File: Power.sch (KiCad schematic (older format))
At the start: 0 parts

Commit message: Power Protection And Filtering
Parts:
- added C? (x2): C, ~, symbol C
- added F? (x4): FUSE, ~, symbol FUSE
- added L? (x2): INDUCTOR, ~, symbol INDUCTOR
- added P?: CONN_12X2, symbol CONN_12X2
- added R?: R, ~, symbol R
- added SW?: SWITCH_INV, ~, symbol SWITCH_INV
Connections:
- net labels added: +12P, +12V, +3.3V, +5V, -12P, -12V, GND
- wire segments 0 -> 34

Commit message: Fan/Current Module Refactoring
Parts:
- removed F? (x4): FUSE, ~, symbol FUSE
- added TH? (x4): THERMISTOR, ~, symbol THERMISTOR
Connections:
- net labels added: +12C
- wire segments 34 -> 35
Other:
- moved on the sheet: R?, SW?
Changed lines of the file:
@@
 Sheet 3 9
 Title ""
-Date "28 sep 2013"
+Date "30 sep 2013"
 Rev ""
 Comp ""
@@
 	1    0    0    -1
 $EndComp
-$Comp
-L FUSE F?
-U 1 1 523E6A3E
-P 2950 1550
-F 0 "F?" H 3050 1600 40  0000 C CNN
-F 1 "FUSE" H 2850 1500 40  0000 C CNN
-F 2 "~" H 2950 1550 60  0000 C CNN
-F 3 "~" H 2950 1550 60  0000 C CNN
-	1    2950 1550
-	1    0    0    -1
-$EndComp
-$Comp
-L FUSE F?
-U 1 1 523E6A4B
-P 3350 1750
-F 0 "F?" H 3450 1800 40  0000 C CNN
-F 1 "FUSE" H 3250 1700 40  0000 C CNN
-F 2 "~" H 3350 1750 60  0000 C CNN
-F 3 "~" H 3350 1750 60  0000 C CNN
-	1    3350 1750
-	1    0    0    -1
-$EndComp
-$Comp
-L FUSE F?
-U 1 1 523E6A51
-P 3750 1950
-F 0 "F?" H 3850 2000 40  0000 C CNN
-F 1 "FUSE" H 3650 1900 40  0000 C CNN
-F 2 "~" H 3750 1950 60  0000 C CNN
-F 3 "~" H 3750 1950 60  0000 C CNN
-	1    3750 1950
-	1    0    0    -1
-$EndComp
-$Comp
-L FUSE F?
-U 1 1 523E6A57
-P 4150 2150
-F 0 "F?" H 4250 2200 40  0000 C CNN
-F 1 "FUSE" H 4050 2100 40  0000 C CNN
-F 2 "~" H 4150 2150 60  0000 C CNN
-F 3 "~" H 4150 2150 60  0000 C CNN
-	1    4150 2150
-	1    0    0    -1
-$EndComp
 Wire Wire Line
 	2350 1550 2700 1550
@@
 L SWITCH_INV SW?
 U 1 1 523E6AF8
-P 3000 2550
-F 0 "SW?" H 2800 2700 50  0000 C CNN
-F 1 "SWITCH_INV" H 2850 2400 50  0000 C CNN
-F 2 "~" H 3000 2550 60  0000 C CNN
-F 3 "~" H 3000 2550 60  0000 C CNN
-	1    3000 2550
+P 3000 2650
+F 0 "SW?" H 2800 2800 50  0000 C CNN
+F 1 "SWITCH_INV" H 2850 2500 50  0000 C CNN
+F 2 "~" H 3000 2650 60  0000 C CNN
+F 3 "~" H 3000 2650 60  0000 C CNN
+	1    3000 2650
 	1    0    0    -1
 $EndComp
@@
 	2350 2250 2500 2250
 Wire Wire Line
-	2500 2250 2500 2550
-Wire Wire Line
-	3500 2650 3650 2650
-Wire Wire Line
-	3650 2650 3650 2800
+	2500 2250 2500 2650
+Wire Wire Line
+	3500 2750 3650 2750
+Wire Wire Line
+	3650 2750 3650 2900
 $Comp
 L GND #PWR?
 U 1 1 523E6DB4
-P 3650 2800
-F 0 "#PWR?" H 3650 2800 30  0001 C CNN
-F 1 "GND" H 3650 2730 30  0001 C CNN
-F 2 "" H 3650 2800 60  0000 C CNN
-F 3 "" H 3650 2800 60  0000 C CNN
-	1    3650 2800
+P 3650 2900
+F 0 "#PWR?" H 3650 2900 30  0001 C CNN
+F 1 "GND" H 3650 2830 30  0001 C CNN
+F 2 "" H 3650 2900 60  0000 C CNN
+F 3 "" H 3650 2900 60  0000 C CNN
+	1    3650 2900
 	1    0    0    -1
 $EndComp
@@
 L R R?
 U 1 1 523E6DE7
-P 3800 2450
-F 0 "R?" V 3880 2450 40  0000 C CNN
-F 1 "R" V 3807 2451 40  0000 C CNN
-F 2 "~" V 3730 2450 30  0000 C CNN
-F 3 "~" H 3800 2450 30  0000 C CNN
-	1    3800 2450
+P 3800 2550
+F 0 "R?" V 3880 2550 40  0000 C CNN
+F 1 "R" V 3807 2551 40  0000 C CNN
+F 2 "~" V 3730 2550 30  0000 C CNN
+F 3 "~" H 3800 2550 30  0000 C CNN
+	1    3800 2550
 	0    -1   -1   0
 $EndComp
@@
 L +3.3V #PWR?
 U 1 1 523E6DF4
-P 4150 2400
-F 0 "#PWR?" H 4150 2360 30  0001 C CNN
-F 1 "+3.3V" H 4150 2510 30  0000 C CNN
-F 2 "" H 4150 2400 60  0000 C CNN
-F 3 "" H 4150 2400 60  0000 C CNN
-	1    4150 2400
-	1    0    0    -1
-$EndComp
-Wire Wire Line
-	3500 2450 3550 2450
-Wire Wire Line
-	4050 2450 4150 2450
-Wire Wire Line
-	4150 2450 4150 2400
+P 4150 2500
+F 0 "#PWR?" H 4150 2460 30  0001 C CNN
+F 1 "+3.3V" H 4150 2610 30  0000 C CNN
+F 2 "" H 4150 2500 60  0000 C CNN
+F 3 "" H 4150 2500 60  0000 C CNN
+	1    4150 2500
+	1    0    0    -1
+$EndComp
+Wire Wire Line
+	3500 2550 3550 2550
+Wire Wire Line
+	4050 2550 4150 2550
+Wire Wire Line
+	4150 2550 4150 2500
 $Comp
 L +12P #PWR?
@@
 Connection ~ 6300 2050
 Connection ~ 6300 3150
+Wire Wire Line
+	2650 1950 2650 1250
+Connection ~ 2650 1950
+$Comp
+L +12C #PWR?
+U 1 1 52493AD5
+P 2650 1250
+F 0 "#PWR?" H 2650 1220 30  0001 C CNN
+F 1 "+12C" H 2650 1360 40  0000 C CNN
+F 2 "" H 2650 1250 60  0000 C CNN
+F 3 "" H 2650 1250 60  0000 C CNN
+	1    2650 1250
+	1    0    0    -1
+$EndComp
+$Comp
+L THERMISTOR TH?
+U 1 1 5249402A
+P 2950 1550
+F 0 "TH?" V 3050 1600 50  0000 C CNN
+F 1 "THERMISTOR" V 2850 1550 50  0000 C CNN
+F 2 "~" H 2950 1550 60  0000 C CNN
+F 3 "~" H 2950 1550 60  0000 C CNN
+	1    2950 1550
+	0    -1   -1   0
+$EndComp
+$Comp
+L THERMISTOR TH?
+U 1 1 52494037
+P 3350 1750
+F 0 "TH?" V 3450 1800 50  0000 C CNN
+F 1 "THERMISTOR" V 3250 1750 50  0000 C CNN
+F 2 "~" H 3350 1750 60  0000 C CNN
+F 3 "~" H 3350 1750 60  0000 C CNN
+	1    3350 1750
+	0    -1   -1   0
+$EndComp
+$Comp
+L THERMISTOR TH?
+U 1 1 5249403D
+P 3750 1950
+F 0 "TH?" V 3850 2000 50  0000 C CNN
+F 1 "THERMISTOR" V 3650 1950 50  0000 C CNN
+F 2 "~" H 3750 1950 60  0000 C CNN
+F 3 "~" H 3750 1950 60  0000 C CNN
+	1    3750 1950
+	0    -1   -1   0
+$EndComp
+$Comp
+L THERMISTOR TH?
+U 1 1 52494043
+P 4150 2150
+F 0 "TH?" V 4250 2200 50  0000 C CNN
+F 1 "THERMISTOR" V 4050 2150 50  0000 C CNN
+F 2 "~" H 4150 2150 60  0000 C CNN
+F 3 "~" H 4150 2150 60  0000 C CNN
+	1    4150 2150
+	0    -1   -1   0
+$EndComp
 $EndSCHEMATC

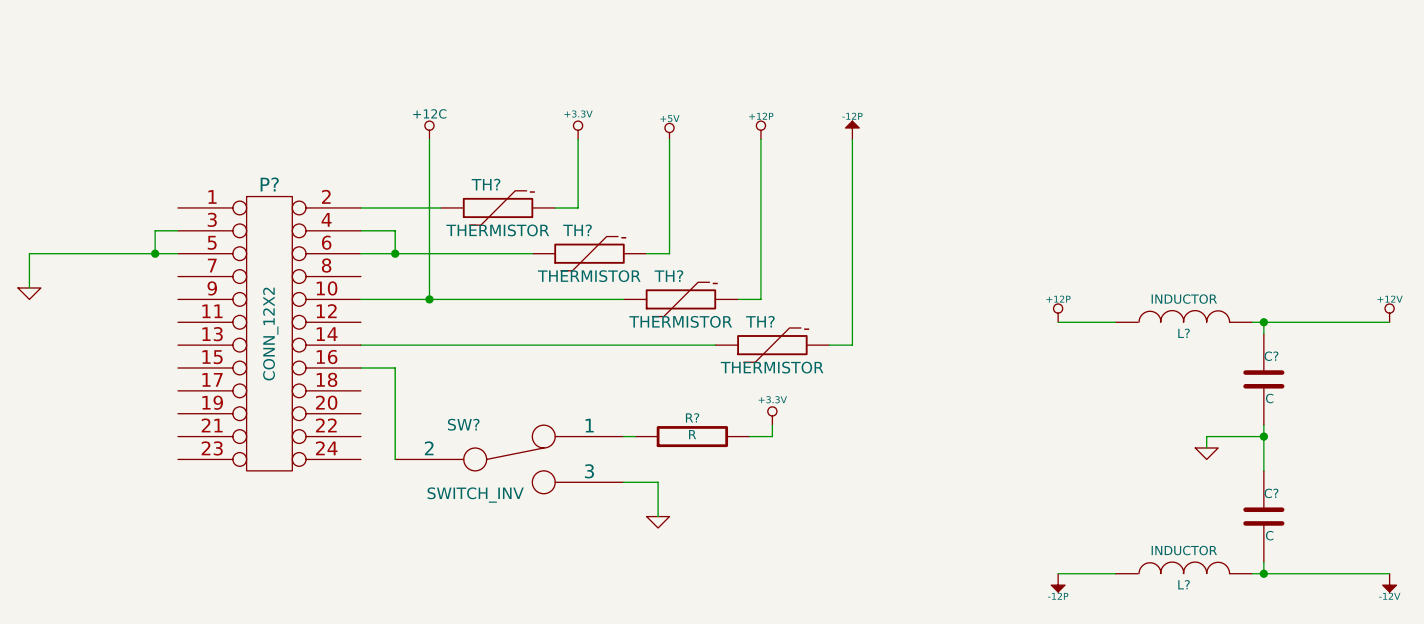
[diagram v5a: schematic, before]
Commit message: Preliminary Module Layouts
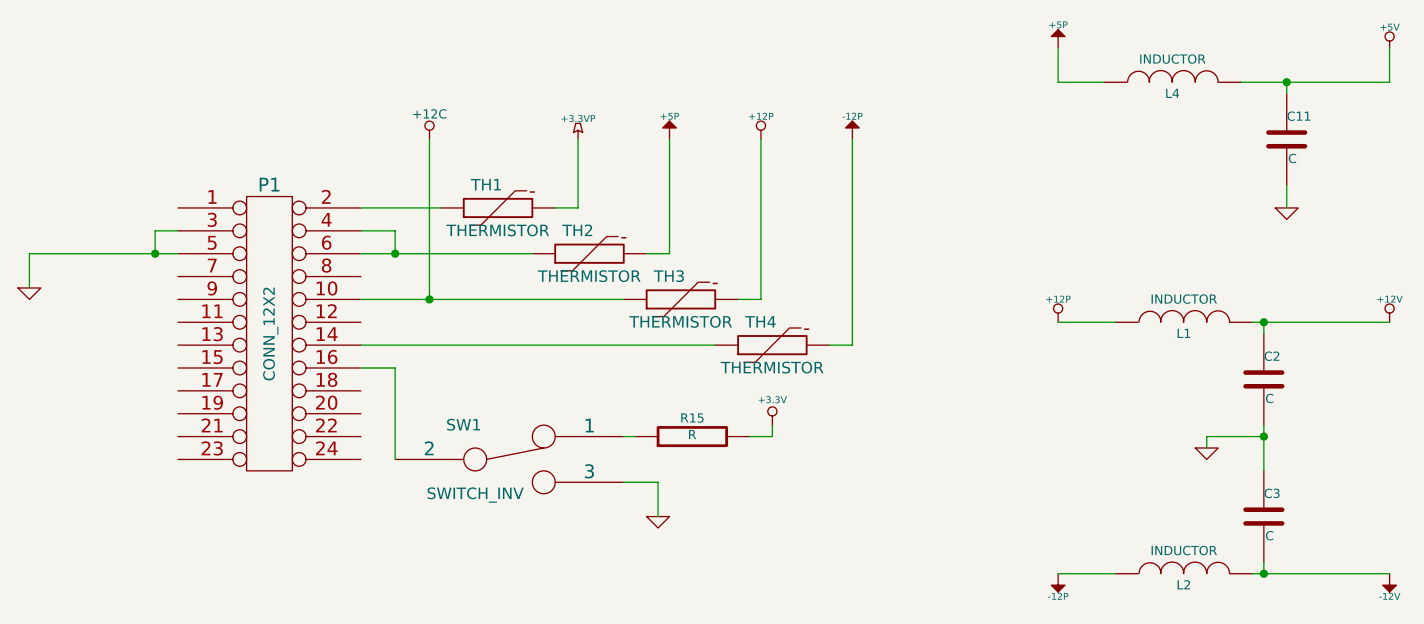
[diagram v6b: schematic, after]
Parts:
- added C11: C, ~, symbol C
- added L4: INDUCTOR, ~, symbol INDUCTOR
- gave numbers to parts that had none: 11
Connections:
- net +3.3V: no longer TH1.2
- net +5V: now also C11.1, L4.2; no longer TH2.2
- net GND: now also C11.2
- new net +3.3VP: TH1.2
- new net +5P: L4.1, TH2.2
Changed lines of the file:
@@
 Sheet 3 9
 Title ""
-Date "30 sep 2013"
+Date "15 oct 2013"
 Rev ""
 Comp ""
@@
 $EndDescr
 $Comp
-L CONN_12X2 P?
+L CONN_12X2 P1
 U 1 1 523E6A2F
 P 1950 2100
-F 0 "P?" H 1950 2750 60  0000 C CNN
+F 0 "P1" H 1950 2750 60  0000 C CNN
 F 1 "CONN_12X2" V 1950 2100 50  0000 C CNN
 F 2 "" H 1950 2100 60  0000 C CNN
@@
 Wire Wire Line
 	3300 1550 3300 1250
-$Comp
-L +3.3V #PWR?
-U 1 1 523E6AA1
-P 3300 1250
-F 0 "#PWR?" H 3300 1210 30  0001 C CNN
-F 1 "+3.3V" H 3300 1360 30  0000 C CNN
-F 2 "" H 3300 1250 60  0000 C CNN
-F 3 "" H 3300 1250 60  0000 C CNN
-	1    3300 1250
-	1    0    0    -1
-$EndComp
 Wire Wire Line
 	3600 1750 3700 1750
 Wire Wire Line
 	3700 1750 3700 1250
-$Comp
-L +5V #PWR?
-U 1 1 523E6ABC
-P 3700 1250
-F 0 "#PWR?" H 3700 1340 20  0001 C CNN
-F 1 "+5V" H 3700 1340 30  0000 C CNN
-F 2 "" H 3700 1250 60  0000 C CNN
-F 3 "" H 3700 1250 60  0000 C CNN
-	1    3700 1250
-	1    0    0    -1
-$EndComp
 Wire Wire Line
 	4000 1950 4100 1950
@@
 	4100 1950 4100 1250
 $Comp
-L +12P #PWR?
+L +12P #PWR018
 U 1 1 523E6AD9
 P 4100 1250
-F 0 "#PWR?" H 4100 1220 30  0001 C CNN
+F 0 "#PWR018" H 4100 1220 30  0001 C CNN
 F 1 "+12P" H 4100 1350 30  0000 C CNN
 F 2 "" H 4100 1250 60  0000 C CNN
@@
 	4500 2150 4500 1250
 $Comp
-L SWITCH_INV SW?
+L SWITCH_INV SW1
 U 1 1 523E6AF8
 P 3000 2650
-F 0 "SW?" H 2800 2800 50  0000 C CNN
+F 0 "SW1" H 2800 2800 50  0000 C CNN
 F 1 "SWITCH_INV" H 2850 2500 50  0000 C CNN
 F 2 "~" H 3000 2650 60  0000 C CNN
@@
 $EndComp
 $Comp
-L -12P #PWR?
+L -12P #PWR019
 U 1 1 523E6B53
 P 4500 1250
-F 0 "#PWR?" H 4500 1380 20  0001 C CNN
+F 0 "#PWR019" H 4500 1380 20  0001 C CNN
 F 1 "-12P" H 4500 1350 30  0000 C CNN
 F 2 "" H 4500 1250 60  0000 C CNN
@@
 Connection ~ 1450 1750
 $Comp
-L GND #PWR?
+L GND #PWR020
 U 1 1 523E6D4C
 P 900 1900
-F 0 "#PWR?" H 900 1900 30  0001 C CNN
+F 0 "#PWR020" H 900 1900 30  0001 C CNN
 F 1 "GND" H 900 1830 30  0001 C CNN
 F 2 "" H 900 1900 60  0000 C CNN
@@
 	3650 2750 3650 2900
 $Comp
-L GND #PWR?
+L GND #PWR021
 U 1 1 523E6DB4
 P 3650 2900
-F 0 "#PWR?" H 3650 2900 30  0001 C CNN
+F 0 "#PWR021" H 3650 2900 30  0001 C CNN
 F 1 "GND" H 3650 2830 30  0001 C CNN
 F 2 "" H 3650 2900 60  0000 C CNN
@@
 $EndComp
 $Comp
-L R R?
+L R R15
 U 1 1 523E6DE7
 P 3800 2550
-F 0 "R?" V 3880 2550 40  0000 C CNN
+F 0 "R15" V 3880 2550 40  0000 C CNN
 F 1 "R" V 3807 2551 40  0000 C CNN
 F 2 "~" V 3730 2550 30  0000 C CNN
@@
 $EndComp
 $Comp
-L +3.3V #PWR?
+L +3.3V #PWR022
 U 1 1 523E6DF4
 P 4150 2500
-F 0 "#PWR?" H 4150 2460 30  0001 C CNN
+F 0 "#PWR022" H 4150 2460 30  0001 C CNN
 F 1 "+3.3V" H 4150 2610 30  0000 C CNN
 F 2 "" H 4150 2500 60  0000 C CNN
@@
 	4150 2550 4150 2500
 $Comp
-L +12P #PWR?
+L +12P #PWR023
 U 1 1 523E7000
 P 5400 2050
-F 0 "#PWR?" H 5400 2020 30  0001 C CNN
+F 0 "#PWR023" H 5400 2020 30  0001 C CNN
 F 1 "+12P" H 5400 2150 30  0000 C CNN
 F 2 "" H 5400 2050 60  0000 C CNN
@@
 $EndComp
 $Comp
-L GND #PWR?
+L GND #PWR024
 U 1 1 523E701E
 P 6050 2600
-F 0 "#PWR?" H 6050 2600 30  0001 C CNN
+F 0 "#PWR024" H 6050 2600 30  0001 C CNN
 F 1 "GND" H 6050 2530 30  0001 C CNN
 F 2 "" H 6050 2600 60  0000 C CNN
@@
 $EndComp
 $Comp
-L INDUCTOR L?
+L INDUCTOR L1
 U 1 1 523E702D
 P 5950 2050
-F 0 "L?" V 5900 2050 40  0000 C CNN
+F 0 "L1" V 5900 2050 40  0000 C CNN
 F 1 "INDUCTOR" V 6050 2050 40  0000 C CNN
 F 2 "~" H 5950 2050 60  0000 C CNN
@@
 $EndComp
 $Comp
-L INDUCTOR L?
+L INDUCTOR L2
 U 1 1 523E703A
 P 5950 3150
-F 0 "L?" V 5900 3150 40  0000 C CNN
+F 0 "L2" V 5900 3150 40  0000 C CNN
 F 1 "INDUCTOR" V 6050 3150 40  0000 C CNN
 F 2 "~" H 5950 3150 60  0000 C CNN
@@
 $EndComp
 $Comp
-L -12P #PWR?
+L -12P #PWR025
 U 1 1 523E7201
 P 5400 3150
-F 0 "#PWR?" H 5400 3280 20  0001 C CNN
+F 0 "#PWR025" H 5400 3280 20  0001 C CNN
 F 1 "-12P" H 5400 3250 30  0000 C CNN
 F 2 "" H 5400 3150 60  0000 C CNN
@@
 $EndComp
 $Comp
-L C C?
+L C C3
 U 1 1 523E7229
 P 6300 2900
-F 0 "C?" H 6300 3000 40  0000 L CNN
+F 0 "C3" H 6300 3000 40  0000 L CNN
 F 1 "C" H 6306 2815 40  0000 L CNN
 F 2 "~" H 6338 2750 30  0000 C CNN
@@
 $EndComp
 $Comp
-L C C?
+L C C2
 U 1 1 523E7236
 P 6300 2300
-F 0 "C?" H 6300 2400 40  0000 L CNN
+F 0 "C2" H 6300 2400 40  0000 L CNN
 F 1 "C" H 6306 2215 40  0000 L CNN
 F 2 "~" H 6338 2150 30  0000 C CNN
@@
 	5650 3150 5400 3150
 $Comp
-L -12V #PWR?
+L -12V #PWR026
 U 1 1 523E7358
 P 6850 3150
-F 0 "#PWR?" H 6850 3280 20  0001 C CNN
+F 0 "#PWR026" H 6850 3280 20  0001 C CNN
 F 1 "-12V" H 6850 3250 30  0000 C CNN
 F 2 "" H 6850 3150 60  0000 C CNN
@@
 $EndComp
 $Comp
-L +12V #PWR?
+L +12V #PWR027
 U 1 1 523E7367
 P 6850 2050
-F 0 "#PWR?" H 6850 2000 20  0001 C CNN
+F 0 "#PWR027" H 6850 2000 20  0001 C CNN
 F 1 "+12V" H 6850 2150 30  0000 C CNN
 F 2 "" H 6850 2050 60  0000 C CNN
@@
 Connection ~ 2650 1950
 $Comp
-L +12C #PWR?
+L +12C #PWR028
 U 1 1 52493AD5
 P 2650 1250
-F 0 "#PWR?" H 2650 1220 30  0001 C CNN
+F 0 "#PWR028" H 2650 1220 30  0001 C CNN
 F 1 "+12C" H 2650 1360 40  0000 C CNN
 F 2 "" H 2650 1250 60  0000 C CNN
@@
 $EndComp
 $Comp
-L THERMISTOR TH?
+L THERMISTOR TH1
 U 1 1 5249402A
 P 2950 1550
-F 0 "TH?" V 3050 1600 50  0000 C CNN
+F 0 "TH1" V 3050 1600 50  0000 C CNN
 F 1 "THERMISTOR" V 2850 1550 50  0000 C CNN
 F 2 "~" H 2950 1550 60  0000 C CNN
@@
 $EndComp
 $Comp
-L THERMISTOR TH?
+L THERMISTOR TH2
 U 1 1 52494037
 P 3350 1750
-F 0 "TH?" V 3450 1800 50  0000 C CNN
+F 0 "TH2" V 3450 1800 50  0000 C CNN
 F 1 "THERMISTOR" V 3250 1750 50  0000 C CNN
 F 2 "~" H 3350 1750 60  0000 C CNN
@@
 $EndComp
 $Comp
-L THERMISTOR TH?
+L THERMISTOR TH3
 U 1 1 5249403D
 P 3750 1950
-F 0 "TH?" V 3850 2000 50  0000 C CNN
+F 0 "TH3" V 3850 2000 50  0000 C CNN
 F 1 "THERMISTOR" V 3650 1950 50  0000 C CNN
 F 2 "~" H 3750 1950 60  0000 C CNN
@@
 $EndComp
 $Comp
-L THERMISTOR TH?
+L THERMISTOR TH4
 U 1 1 52494043
 P 4150 2150
-F 0 "TH?" V 4250 2200 50  0000 C CNN
+F 0 "TH4" V 4250 2200 50  0000 C CNN
 F 1 "THERMISTOR" V 4050 2150 50  0000 C CNN
 F 2 "~" H 4150 2150 60  0000 C CNN
@@
 	0    -1   -1   0
 $EndComp
+$Comp
+L +5P #PWR26
+U 1 1 525B1C96
+P 5400 850
+F 0 "#PWR26" H 5400 980 20  0001 C CNN
+F 1 "+5P" H 5400 950 30  0000 C CNN
+F 2 "" H 5400 850 60  0000 C CNN
+F 3 "" H 5400 850 60  0000 C CNN
+	1    5400 850
+	1    0    0    -1
+$EndComp
+$Comp
+L +5V #PWR029
+U 1 1 525B1CA5
+P 6850 850
+F 0 "#PWR029" H 6850 940 20  0001 C CNN
+F 1 "+5V" H 6850 940 30  0000 C CNN
+F 2 "" H 6850 850 60  0000 C CNN
+F 3 "" H 6850 850 60  0000 C CNN
+	1    6850 850
+	1    0    0    -1
+$EndComp
+$Comp
+L GND #PWR030
+U 1 1 525B1CB4
+P 6400 1550
+F 0 "#PWR030" H 6400 1550 30  0001 C CNN
+F 1 "GND" H 6400 1480 30  0001 C CNN
+F 2 "" H 6400 1550 60  0000 C CNN
+F 3 "" H 6400 1550 60  0000 C CNN
+	1    6400 1550
+	1    0    0    -1
+$EndComp
+$Comp
+L INDUCTOR L4
+U 1 1 525B1CC3
+P 5900 1000
+F 0 "L4" V 5850 1000 40  0000 C CNN
+F 1 "INDUCTOR" V 6000 1000 40  0000 C CNN
+F 2 "~" H 5900 1000 60  0000 C CNN
+F 3 "~" H 5900 1000 60  0000 C CNN
+	1    5900 1000
+	0    -1   -1   0
+$EndComp
+Wire Wire Line
+	5400 850  5400 1000
+Wire Wire Line
+	5400 1000 5600 1000
+Wire Wire Line
+	6200 1000 6850 1000
+Wire Wire Line
+	6850 1000 6850 850
+$Comp
+L C C11
+U 1 1 525B1D28
+P 6400 1250
+F 0 "C11" H 6400 1350 40  0000 L CNN
+F 1 "C" H 6406 1165 40  0000 L CNN
+F 2 "~" H 6438 1100 30  0000 C CNN
+F 3 "~" H 6400 1250 60  0000 C CNN
+	1    6400 1250
+	1    0    0    -1
+$EndComp
+Wire Wire Line
+	6400 1050 6400 1000
+Connection ~ 6400 1000
+Wire Wire Line
+	6400 1450 6400 1550
+$Comp
+L +3.3VP #PWR031
+U 1 1 525C49D8
+P 3300 1250
+F 0 "#PWR031" H 3350 1280 20  0001 C CNN
+F 1 "+3.3VP" H 3300 1340 30  0000 C CNN
+F 2 "" H 3300 1250 60  0000 C CNN
+F 3 "" H 3300 1250 60  0000 C CNN
+	1    3300 1250
+	1    0    0    -1
+$EndComp
+$Comp
+L +5P #PWR22
+U 1 1 525C49F1
+P 3700 1250
+F 0 "#PWR22" H 3700 1380 20  0001 C CNN
+F 1 "+5P" H 3700 1350 30  0000 C CNN
+F 2 "" H 3700 1250 60  0000 C CNN
+F 3 "" H 3700 1250 60  0000 C CNN
+	1    3700 1250
+	1    0    0    -1
+$EndComp
 $EndSCHEMATC

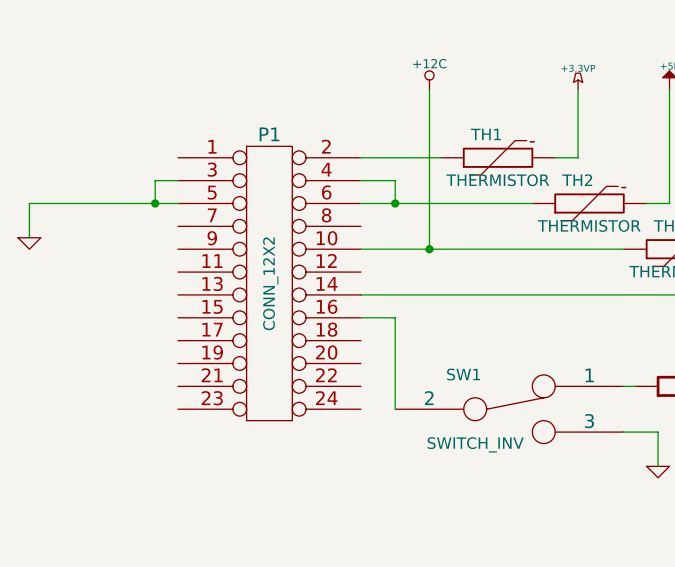
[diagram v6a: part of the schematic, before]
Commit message: Plug Placement
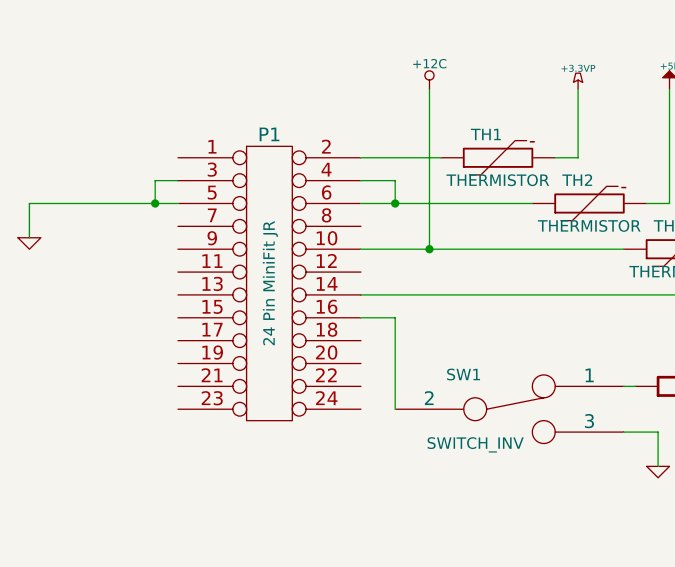
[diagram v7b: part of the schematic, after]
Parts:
- P1: value CONN_12X2 -> 24 Pin MiniFit JR
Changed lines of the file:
@@
 Sheet 3 9
 Title ""
-Date "15 oct 2013"
+Date "17 oct 2013"
 Rev ""
 Comp ""
@@
 P 1950 2100
 F 0 "P1" H 1950 2750 60  0000 C CNN
-F 1 "CONN_12X2" V 1950 2100 50  0000 C CNN
+F 1 "24 Pin MiniFit JR" V 1950 2100 50  0000 C CNN
 F 2 "" H 1950 2100 60  0000 C CNN
 F 3 "" H 1950 2100 60  0000 C CNN
